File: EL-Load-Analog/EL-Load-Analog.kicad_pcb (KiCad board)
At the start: 4 copper layers, 185 x 95 mm, 282 parts, among them J1 Fan PWM, J101 Conn_01x10_Male, J102 JST-XH 2-pin, J103 JST-XH 2-pin, J104 Conn_02x12_Counter_Clockwise, J301 VSense, Q101 TIP42C, Q201 2N7002, Q202 2N7002, Q203 IRFP250M, Q204 IRFP250M, Q205 2N7002, Q206 2N7002, Q207 IRFP250M, Q208 IRFP250M, Q301 2N7002, Q302 BSS138, Q401 BSS138, U1 ADS1115IDGS, U101 AMS1117-3.3, U102 ADM1032, U2 MAX31760, U201 LM318D, U202 LM318D, U203 MCP6V51/LTC2050HV, U204 MCP6V51/LTC2050HV, U205 LM318D, U206 LM318D, U207 MCP6V51/LTC2050HV, U208 MCP6V51/LTC2050HV, U3 BD00FC0WFP-E2, U301 LM833, U302 LM833, U303 OPA189/MCP6V51/LTC2050HV, U304 OPA189/MCP6V51/LTC2050HV, U305 74HCT02, U306 LM393, U401 AD8038, U402 LM393, U403 74HCT02, U501 TL431DBZ, U502 TL074, U503 TL074, U504 TL072

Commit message: Put REF2025 in place, added LICENSES and .gitignore
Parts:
- removed C105: 10u, Capacitor_SMD:C_0805_2012Metric_Pad1.18x1.45mm_HandSolder
- removed C106: 100n, Capacitor_SMD:C_0805_2012Metric_Pad1.18x1.45mm_HandSolder
- removed J102, J103: JST-XH 2-pin, Connector_JST:JST_XH_B2B-XH-A_1x02_P2.50mm_Vertical
- removed R501: 100, Resistor_SMD:R_0805_2012Metric_Pad1.20x1.40mm_HandSolder
- removed U501: TL431DBZ, Package_TO_SOT_SMD:SOT-23
- added C10: 1u, Capacitor_SMD:C_0805_2012Metric_Pad1.18x1.45mm_HandSolder, F.Cu at (76.2, 113.7)
- added C11: 22u, Capacitor_SMD:C_0805_2012Metric_Pad1.18x1.45mm_HandSolder, F.Cu at (88.0, 111.0)
- added C12: 1u, Capacitor_SMD:C_0805_2012Metric_Pad1.18x1.45mm_HandSolder, F.Cu at (93.0, 109.0)
- added U4: REF5025AD, Package_SO:SOIC-8_3.9x4.9mm_P1.27mm, F.Cu at (83.2, 112.0)
- moved C503 4.39 mm to (93.8, 112.8), turned to 90 degrees
- moved R502 1.42 mm to (95.2, 109.0)
- moved R504 1.34 mm to (97.1, 109.0)
- moved R506 1.33 mm to (101.2, 109.0)
- moved C504 1.31 mm to (99.1, 109.0)
- moved R508 1.25 mm to (103.1, 109.0)
- moved C508 1.00 mm to (90.2, 108.9)
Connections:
- C503 pad 1: Vref -> Net-(U4-Trim/NR)
- U502 pad 1: Vref -> unconnected-(U502-Pad1)
- U502 pad 2: Vref -> unconnected-(U502A---Pad2)
- U502 pad 3: Net-(U501-K) -> unconnected-(U502A-+-Pad3)
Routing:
- net +12P: track 329.3 -> 137.2 mm, vias 5 -> 4
- net Net-(U501-K): track 17.8 -> 0.00 mm, vias 2 -> 0
- net +5V: track 560.2 -> 576.3 mm, vias 19 -> 21
- net GND: track 399.6 -> 389.5 mm, vias 145 -> 149
- net Vref: track 43.5 -> 53.3 mm
- net Net-(U4-Trim/NR): track 0.00 -> 8.10 mm
- net SCL: track 188.6 -> 193.2 mm, vias 2 -> 4
- net Net-(U502B-+): track 21.2 -> 19.8 mm
- net -GCOM: track 165.8 -> 164.5 mm
- net +3.3V: track 459.9 -> 459.3 mm

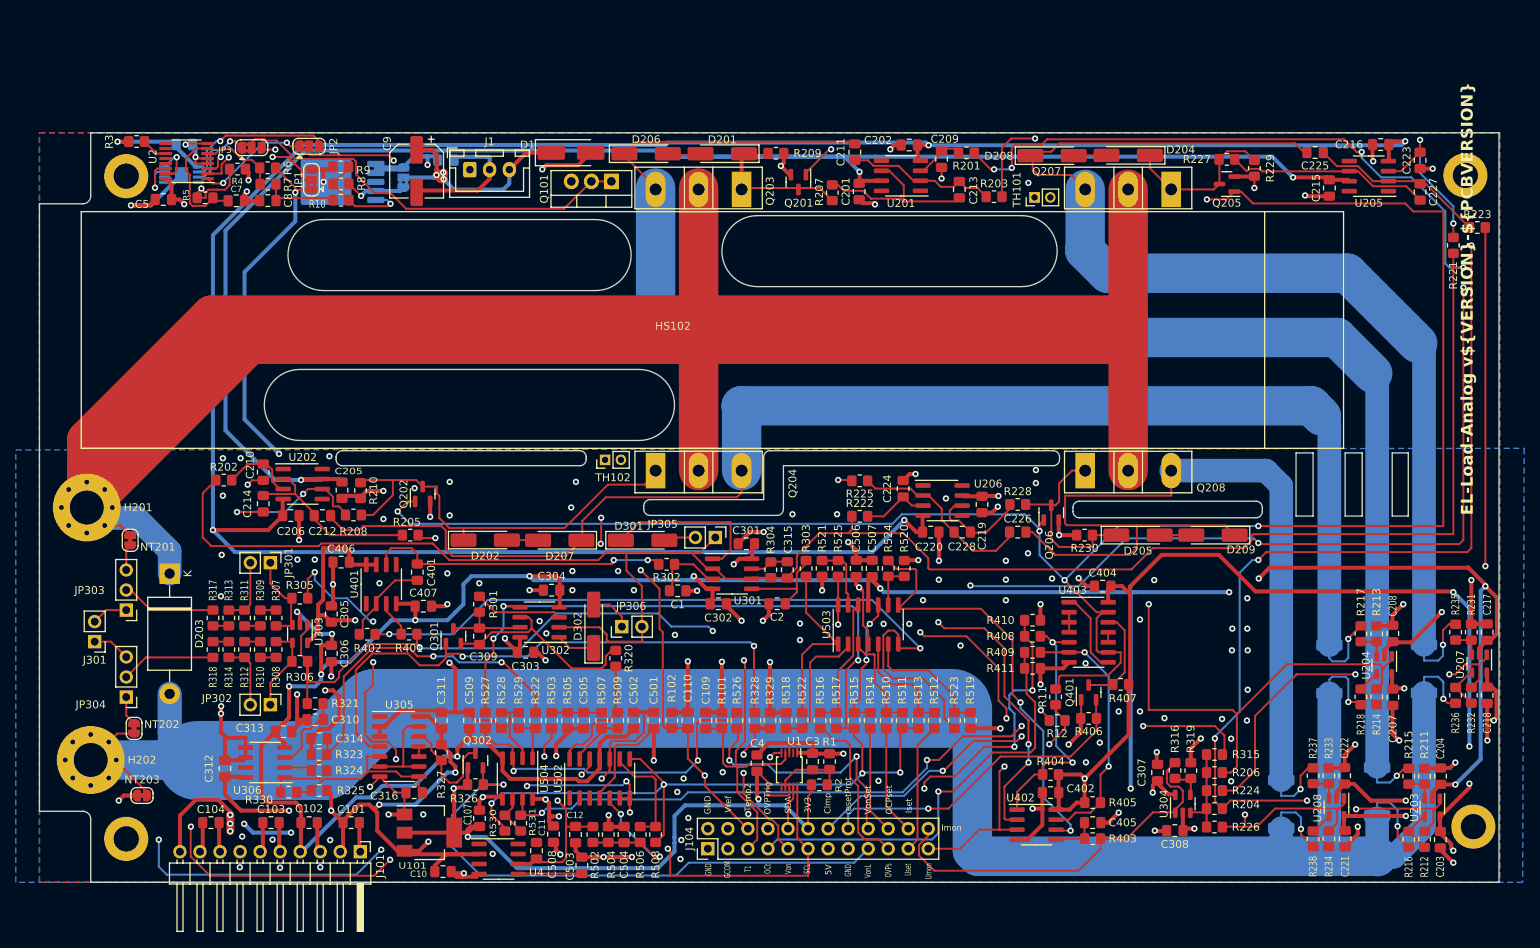
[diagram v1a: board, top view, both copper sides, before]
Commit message: Major Analog PCB update DAC/ADC + connectors included, fan IC removed
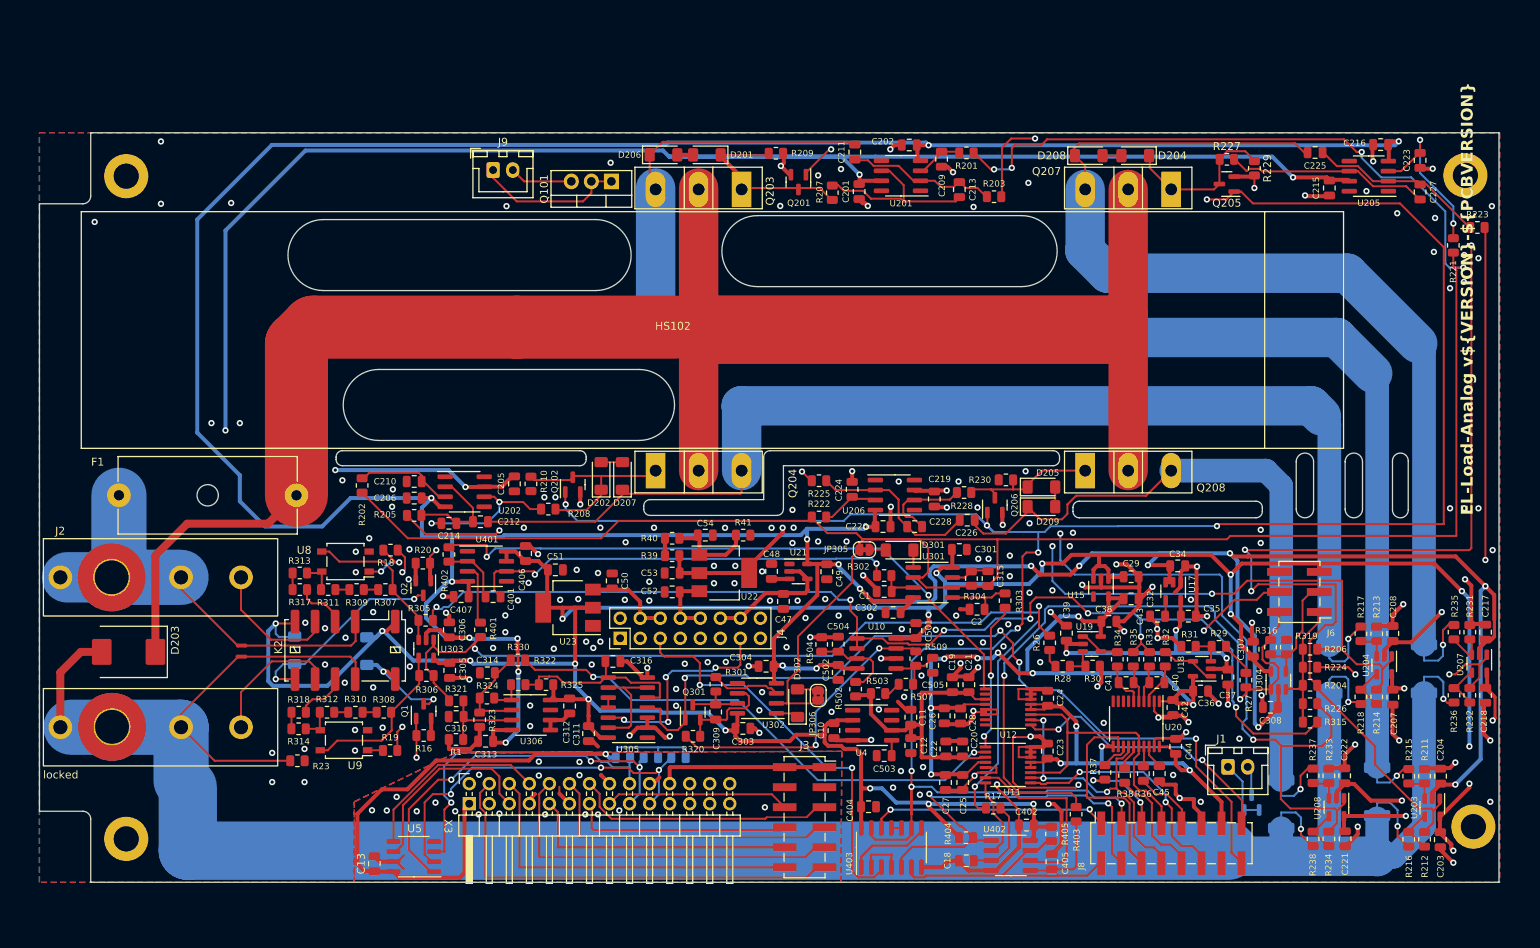
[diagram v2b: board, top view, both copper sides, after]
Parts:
- removed C101, C102, C103, C104, C107: 10u, Capacitor_SMD:C_0805_2012Metric_Pad1.18x1.45mm_HandSolder
- removed C108, C4, C5, C506, C507, C508, C509, C7: 100n, Capacitor_SMD:C_0805_2012Metric_Pad1.18x1.45mm_HandSolder
- removed C109, C110, C3, C6: 10n, Capacitor_SMD:C_0805_2012Metric_Pad1.18x1.45mm_HandSolder
- removed C8: 1u, Capacitor_SMD:C_0805_2012Metric_Pad1.18x1.45mm_HandSolder
- removed C9: 10u, Capacitor_SMD:CP_Elec_6.3x5.8
- removed D1: SS14, Diode_SMD:D_SMA_Handsoldering
- removed J101: Conn_01x10_Male, Connector_PinHeader_2.54mm:PinHeader_1x10_P2.54mm_Horizontal
- removed J104: Conn_02x12_Counter_Clockwise, Connector_PinHeader_2.54mm:PinHeader_2x12_P2.54mm_Vertical
- removed J301: VSense, Connector_PinHeader_2.54mm:PinHeader_1x02_P2.54mm_Vertical
- removed JP1: I2C Address, Jumper:SolderJumper-3_P1.3mm_Bridged2Bar12_RoundedPad1.0x1.5mm
- removed JP2, JP3, JP4: SolderJumper_3_Bridged12, Jumper:SolderJumper-3_P1.3mm_Bridged2Bar12_RoundedPad1.0x1.5mm
- removed JP301, JP302: Jumper_2_Open, Connector_PinHeader_2.54mm:PinHeader_1x02_P2.54mm_Vertical
- removed JP303, JP304: Jumper_3_Open, Connector_PinHeader_2.54mm:PinHeader_1x03_P2.54mm_Vertical
- removed NT203: NetTie_2, Jumper:SolderJumper-2_P1.3mm_Bridged_RoundedPad1.0x1.5mm
- removed Q302, Q401: BSS138, Package_TO_SOT_SMD:SOT-23
- removed R10, R101, R102, R9: 3k3, Resistor_SMD:R_0805_2012Metric_Pad1.20x1.40mm_HandSolder
- removed R11, R326, R327, R328, R406, R407, R408, R409, R506, R508, R510, R511, R512, R513, R514, R515, R516, R517, R518, R519, R520, R521, R522, R523, R524, R525, R526, R527, R528, R529: 10k, Resistor_SMD:R_0805_2012Metric_Pad1.20x1.40mm_HandSolder
- removed R12, R329, R410, R411, R530, R531: 20k, Resistor_SMD:R_0805_2012Metric_Pad1.20x1.40mm_HandSolder
- removed R2: 6k8, Resistor_SMD:R_0805_2012Metric_Pad1.20x1.40mm_HandSolder
- removed R3, R6: 4k7, Resistor_SMD:R_0805_2012Metric_Pad1.20x1.40mm_HandSolder
- removed R4, R7: 1k, Resistor_SMD:R_0805_2012Metric_Pad1.20x1.40mm_HandSolder
- removed R5: 10, Resistor_SMD:R_0805_2012Metric_Pad1.20x1.40mm_HandSolder
- removed R505: 15k, Resistor_SMD:R_0805_2012Metric_Pad1.20x1.40mm_HandSolder
- removed R8: 39k, Resistor_SMD:R_0805_2012Metric_Pad1.20x1.40mm_HandSolder
- removed TH101, TH102: Thermistor_NTC 10k, Connector_PinHeader_2.00mm:PinHeader_1x02_P2.00mm_Vertical
- removed U1: ADS1115IDGS, Package_SO:TSSOP-10_3x3mm_P0.5mm
- removed U101: AMS1117-3.3, Package_TO_SOT_SMD:SOT-223-3_TabPin2
- removed U102: ADM1032, Package_SO:MSOP-8-1EP_3x3mm_P0.65mm_EP1.68x1.88mm
- removed U2: MAX31760, Package_SO:QSOP-16_3.9x4.9mm_P0.635mm
- removed U3: BD00FC0WFP-E2, Package_TO_SOT_SMD:TO-252-5_TabPin6
- removed U502, U503: TL074, Package_SO:SO-14_3.9x8.65mm_P1.27mm
- removed U504: TL072, Package_SO:SO-8_3.9x4.9mm_P1.27mm
- added C13: 100n, Capacitor_SMD:C_0805_2012Metric, F.Cu at (67.5, 112.7)
- added C18: 10n, Capacitor_SMD:C_0805_2012Metric, F.Cu at (142.5, 112.3)
- added C19: 1u, Capacitor_SMD:C_0805_2012Metric, F.Cu at (140.7, 90.0)
- added C20: 1u, Capacitor_SMD:C_0805_2012Metric, F.Cu at (142.0, 98.1)
- added C21: 100n, Capacitor_SMD:C_0805_2012Metric, F.Cu at (142.8, 90.0)
- added C22: 100n, Capacitor_SMD:C_0805_2012Metric, F.Cu at (139.9, 98.1)
- added C23: 100n, Capacitor_SMD:C_0805_2012Metric, F.Cu at (152.8, 98.4)
- added C24: 100n, Capacitor_SMD:C_0805_2012Metric, F.Cu at (152.8, 91.7)
- added C25: 100n, Capacitor_SMD:C_0805_2012Metric, F.Cu at (142.0, 102.3)
- added C26: 100n, Capacitor_SMD:C_0805_2012Metric, F.Cu at (139.7, 93.9)
- added C27: 10u, Capacitor_SMD:C_0805_2012Metric, F.Cu at (139.8, 102.3)
- added C28: 10u, Capacitor_SMD:C_0805_2012Metric, F.Cu at (141.8, 93.9)
- added C29: 1u, Capacitor_SMD:C_0805_2012Metric, F.Cu at (163.4, 76.3)
- added C32: 1u, Capacitor_SMD:C_0805_2012Metric, F.Cu at (163.4, 79.1)
- added C34: 2u2, Capacitor_SMD:C_0805_2012Metric, F.Cu at (169.3, 74.9)
- added C35: 2u2, Capacitor_SMD:C_0805_2012Metric, F.Cu at (170.6, 81.3)
- added C36: 100n, Capacitor_SMD:C_0805_2012Metric, F.Cu at (172.2, 90.8)
- added C37: 100n, Capacitor_SMD:C_0805_2012Metric, F.Cu at (175.7, 89.0)
- added C38: 100n, Capacitor_SMD:C_0805_2012Metric, F.Cu at (160.6, 81.9)
- added C39: 100n, Capacitor_SMD:C_0805_2012Metric, F.Cu at (155.2, 83.4)
- added C40: 10n, Capacitor_SMD:C_0805_2012Metric, F.Cu at (166.6, 89.7)
- added C41: 10n, Capacitor_SMD:C_0805_2012Metric, F.Cu at (162.7, 89.7)
- added C42: 1u, Capacitor_SMD:C_0805_2012Metric, F.Cu at (168.7, 92.8)
- added C43: 10n, Capacitor_SMD:C_0805_2012Metric, F.Cu at (166.7, 81.3)
- added C44: 1u, Capacitor_SMD:C_0805_2012Metric, F.Cu at (169.0, 97.8)
- added C45: 220n, Capacitor_SMD:C_0805_2012Metric, F.Cu at (166.9, 101.2)
- added C47: 1u, Capacitor_SMD:C_0805_2012Metric, F.Cu at (119.3, 79.4)
- added C48: 10n, Capacitor_SMD:C_0805_2012Metric, F.Cu at (117.8, 75.6)
- added C49: 10u, Capacitor_SMD:C_0805_2012Metric, F.Cu at (124.8, 75.6)
- added C50: 10u, Capacitor_SMD:C_0805_2012Metric, F.Cu at (97.6, 76.8)
- added C51: 22u, Capacitor_SMD:C_0805_2012Metric, F.Cu at (90.4, 75.4)
- added C52: 10u, Capacitor_SMD:C_0805_2012Metric, F.Cu at (105.2, 78.2)
- added C53: 22u, Capacitor_SMD:C_0805_2012Metric, F.Cu at (105.2, 75.8)
- added C54: 10n, Capacitor_SMD:C_0805_2012Metric, F.Cu at (109.4, 71.0)
- added D2: 1N4148, Diode_SMD:D_MiniMELF, B.Cu at (66.5, 85.7)
- added D3: 1N4148, Diode_SMD:D_MiniMELF, B.Cu at (57.4, 85.6)
- added F1: Fuse, Fuse:Fuseholder_Cylinder-5x20mm_Schurter_0031_8201_Horizontal_Open, F.Cu at (35.1, 66.0)
- added J2: Plus Terminal w. sense, Footprints:Deltron_Dual_4mm_572_0x00, F.Cu at (27.6, 76.3)
- added J3: Conn_02x06_Odd_Even, Connector_PinSocket_2.54mm:PinSocket_2x06_P2.54mm_Vertical_SMD, F.Cu at (122.0, 106.8)
- added J4: Conn_02x08_Odd_Even, Connector_PinHeader_2.54mm:PinHeader_2x08_P2.54mm_Vertical, F.Cu at (98.6, 84.1)
- added J6: Conn_02x03_Counter_Clockwise, Connector_PinHeader_2.54mm:PinHeader_2x03_P2.54mm_Vertical_SMD, F.Cu at (184.7, 78.2)
- added J8: Conn_02x08_Odd_Even, Connector_PinSocket_2.54mm:PinSocket_2x08_P2.54mm_Vertical_SMD, F.Cu at (168.5, 110.0)
- added J9: Temp Sensor heatsink, Connector_JST:JST_XH_B2B-XH-A_1x02_P2.50mm_Vertical, F.Cu at (82.5, 24.7)
- added K2: EE2-5TNU, Relay_SMD:Relay_DPDT_Kemet_EE2_NU_DoubleCoil, F.Cu at (63.8, 85.6)
- added Q1: 2N7002, Package_TO_SOT_SMD:SOT-23, F.Cu at (73.7, 93.3)
- added Q2: 2N7002, Package_TO_SOT_SMD:SOT-23, F.Cu at (73.7, 77.7)
- added Q4: MMBT3904, Package_TO_SOT_SMD:SOT-23, B.Cu at (178.7, 104.9)
- added R13: 10k, Resistor_SMD:R_0805_2012Metric, B.Cu at (102.5, 99.2)
- added R14: 10k, Resistor_SMD:R_0805_2012Metric, B.Cu at (106.0, 99.2)
- added R15: 10k, Resistor_SMD:R_0805_2012Metric, B.Cu at (99.0, 99.2)
- added R16: 100k, Resistor_SMD:R_0805_2012Metric, F.Cu at (73.7, 96.4)
- added R17: 10k, Resistor_SMD:R_0805_2012Metric, F.Cu at (145.9, 105.6)
- added R18: 100k, Resistor_SMD:R_0805_2012Metric, F.Cu at (69.5, 72.9)
- added R19: 100k, Resistor_SMD:R_0805_2012Metric, F.Cu at (69.5, 98.3)
- added R20: 100k, Resistor_SMD:R_0805_2012Metric, F.Cu at (73.6, 74.5)
- added R23: 0, Resistor_SMD:R_0805_2012Metric, F.Cu at (57.7, 99.6)
- added R26: 100k 0.1%, Resistor_SMD:R_0805_2012Metric, F.Cu at (153.1, 84.7)
- added R27: 100k 0.1%, Resistor_SMD:R_0805_2012Metric, F.Cu at (177.9, 89.4)
- added R28: 10k 0.1%, Resistor_SMD:R_0805_2012Metric, F.Cu at (154.7, 87.6)
- added R29: 10k 0.1%, Resistor_SMD:R_0805_2012Metric, F.Cu at (174.5, 85.1)
- added R30: 100k 0.1%, Resistor_SMD:R_0805_2012Metric, F.Cu at (158.5, 87.6)
- added R31: 100k 0.1%, Resistor_SMD:R_0805_2012Metric, F.Cu at (170.7, 85.1)
- added R32: 1k, Resistor_SMD:R_0805_2012Metric, F.Cu at (167.7, 86.7)
- added R33: 1k, Resistor_SMD:R_0805_2012Metric, F.Cu at (165.7, 86.7)
- added R34: 1k, Resistor_SMD:R_0805_2012Metric, F.Cu at (161.6, 86.7)
- added R35: 1k, Resistor_SMD:R_0805_2012Metric, F.Cu at (163.7, 86.7)
- added R36: 47, Resistor_SMD:R_0805_2012Metric, F.Cu at (164.9, 101.2)
- added R37: 47, Resistor_SMD:R_0805_2012Metric, F.Cu at (160.1, 101.1)
- added R38: 47, Resistor_SMD:R_0805_2012Metric, F.Cu at (162.6, 101.5)
- added R39: 91, Resistor_SMD:R_0805_2012Metric, F.Cu at (105.2, 73.6)
- added R40: 1k8, Resistor_SMD:R_0805_2012Metric, F.Cu at (105.2, 71.4)
- added R41: 220, Resistor_SMD:R_0805_2012Metric, F.Cu at (114.2, 71.0)
- added U10: TL072/OPA2376, Package_SO:SOIC-8_3.9x4.9mm_P1.27mm, F.Cu at (131.1, 86.0)
- added U11: DAC8555, Package_SO:TSSOP-16_4.4x5mm_P0.65mm, F.Cu at (147.8, 100.1)
- added U12: DAC8555, Package_SO:TSSOP-16_4.4x5mm_P0.65mm, F.Cu at (147.8, 92.8)
- added U15: TPS7A2030, Package_TO_SOT_SMD:SOT-23-5, F.Cu at (159.6, 77.7)
- added U17: TPS72325, Package_TO_SOT_SMD:SOT-23-5, F.Cu at (168.7, 78.1)
- added U18: MCP6V51, Package_TO_SOT_SMD:SOT-23-5, F.Cu at (172.3, 87.9)
- added U19: MCP6V51, Package_TO_SOT_SMD:SOT-23-5, F.Cu at (158.4, 84.8)
- added U20: ADS131M02, Package_SO:TSSOP-20_4.4x6.5mm_P0.65mm, F.Cu at (164.0, 94.9)
- added U21: LT1964-5, Package_TO_SOT_SMD:TSOT-23-5, F.Cu at (121.2, 75.6)
- added U22: AMS1117, Package_TO_SOT_SMD:SOT-223-3_TabPin2, F.Cu at (111.8, 75.8)
- added U23: TLV1117-50, Package_TO_SOT_SMD:SOT-223-3_TabPin2, F.Cu at (92.0, 80.2)
- added U5: 24LC32, Package_SO:SO-8_3.9x4.9mm_P1.27mm, F.Cu at (72.5, 111.8)
- added U8: VO1400AEFTR, Package_SO:SO-4_4.4x4.3mm_P2.54mm, F.Cu at (63.8, 74.3)
- added U9: VO1400AEFTR, Package_SO:SO-4_4.4x4.3mm_P2.54mm, F.Cu at (63.6, 97.0)
- added X3: DIB Pheriperal connector, EEZ-DIB:DIB Pheriperal connector, F.Cu at (79.5, 105.1)
- added locked: Minus Terminal w. sense, Footprints:Deltron_Dual_4mm_572_0x00, F.Cu at (27.6, 95.3)
- C1, C10, C11, C12, C2, C201, C202, C203, C204, C205, C206, C207, C208, C209, C210, C211, C212, C213, C214, C215, C216, C217, C218, C219, C220, C221, C222, C223, C224, C225, C226, C227, C228, C301, C302, C303, C304, C305, C306, C307, C308, C309, C310, C311, C312, C313, C314, C315, C316, C401, C402, C404, C405, C406, C407, C501, C502, C503, C504, C505: footprint Capacitor_SMD:C_0805_2012Metric_Pad1.18x1.45mm_HandSolder -> Capacitor_SMD:C_0805_2012Metric
- D201, D202, D204, D205, D206, D207, D208, D209, D301, D302: footprint Diode_SMD:D_MiniMELF_Handsoldering -> Diode_SMD:D_MiniMELF
- D203: value 1.5KE100A -> 1.5KE100A smd variant; footprint Diode_THT:D_DO-201AE_P15.24mm_Horizontal -> Diode_SMD:D_SMC
- H201, H202: footprint MountingHole:MountingHole_4.3mm_M4_Pad_Via -> MountingHole:MountingHole_4.3mm_M4_Pad_TopBottom
- J1: value Fan PWM -> Temp Sensor PCB; footprint Connector_JST:JST_XH_B3B-XH-A_1x03_P2.50mm_Vertical -> Connector_JST:JST_XH_B2B-XH-A_1x02_P2.50mm_Vertical
- JP305: footprint Connector_PinHeader_2.54mm:PinHeader_1x02_P2.54mm_Vertical -> Jumper:SolderJumper-2_P1.3mm_Bridged_RoundedPad1.0x1.5mm
- JP306: footprint Connector_PinHeader_2.54mm:PinHeader_1x02_P2.54mm_Vertical -> Jumper:SolderJumper-2_P1.3mm_Bridged2Bar_RoundedPad1.0x1.5mm
- NT201, NT202: footprint Jumper:SolderJumper-2_P1.3mm_Bridged_RoundedPad1.0x1.5mm -> NetTie:NetTie-2_SMD_Pad0.5mm
- R1: value 3k3 -> 100k; footprint Resistor_SMD:R_0805_2012Metric_Pad1.20x1.40mm_HandSolder -> Resistor_SMD:R_0805_2012Metric
- R201, R202, R203, R204, R205, R206, R207, R208, R209, R210, R211, R212, R213, R214, R215, R216, R217, R218, R221, R222, R223, R224, R225, R226, R227, R228, R229, R230, R231, R232, R233, R234, R235, R236, R237, R238, R301, R302, R303, R304, R305, R306, R307, R308, R309, R310, R311, R312, R313, R314, R315, R316, R317, R318, R319, R320, R321, R322, R323, R324, R325, R330, R401, R402, R403, R404, R405, R502, R503, R504, R507, R509: footprint Resistor_SMD:R_0805_2012Metric_Pad1.20x1.40mm_HandSolder -> Resistor_SMD:R_0805_2012Metric
- moved J1 122.3 mm to (175.7, 100.4)
- moved C10 52.7 mm to (125.7, 95.8), turned to -90 degrees
- moved C11 50.4 mm to (135.4, 94.1)
- moved U4 50.3 mm to (130.6, 95.1)
- moved R1 47.4 mm to (77.8, 96.9), turned to 0 degrees
- moved C505 44.8 mm to (138.2, 87.5)
- moved C312 44.4 mm to (92.2, 92.7), turned to 90 degrees
- moved C12 44.0 mm to (135.4, 97.7)
- moved R503 41.5 mm to (131.3, 91.1), turned to 0 degrees
- moved C404 40.8 mm to (130.1, 105.4), turned to 180 degrees
- moved C503 40.8 mm to (132.1, 99.0), turned to 180 degrees
- moved R507 38.8 mm to (134.8, 89.9), turned to 0 degrees
- moved R509 38.6 mm to (136.1, 86.7)
- moved R502 38.1 mm to (128.4, 90.5), turned to 90 degrees
- moved U403 37.0 mm to (133.0, 110.6), turned to 90 degrees
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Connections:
- net LoopImon renamed /MOSFET Loops/LoopImon
- net LoopIset renamed /MOSFET Loops/LoopIset
- C202 pad 1: -5VA -> -5V
- C206 pad 1: -5VA -> -5V
- C216 pad 1: -5VA -> -5V
- C220 pad 1: -5VA -> -5V
- C505 pad 1: Net-(C505-Pad1) -> Net-(U10B-+)
- H201 pad 1: LoadPlus -> /MOSFET Loops/Plus
- J1 pad 1: /Tacho -> Net-(J1-Pin_1)
- J1 pad 2: GND -> Net-(J1-Pin_2)
- NT201 pad 2: LoadPlus -> /MOSFET Loops/Plus
- Q301 pad 1: Net-(Q301-G) -> ~{Von}
- R1 pad 2: Net-(U1-AIN3) -> Net-(U306A-+)
- R303 pad 2: CCsetOut -> Iset
- R315 pad 2: 4GCOM -> GCOM
- R322 pad 1: VonsetComp -> Vonset
- R402 pad 1: CVsetIn -> Uset
- R404 pad 1: Net-(R404-Pad1) -> OVPtriggered
- R405 pad 1: Net-(R405-Pad1) -> OCPtriggered
- R503 pad 2: Net-(C505-Pad1) -> Net-(R503-Pad2)
- R507 pad 1: Net-(C505-Pad1) -> Net-(R503-Pad2)
- R507 pad 2: Net-(U502D--) -> Net-(U10B-+)
- R509 pad 1: Net-(U502D--) -> Net-(U10B-+)
- U201 pad 4: -5VA -> -5V
- U202 pad 4: -5VA -> -5V
- U205 pad 4: -5VA -> -5V
- U206 pad 4: -5VA -> -5V
- U302 pad 5: -GCOM -> GND
- U305 pad 12: Net-(Q302-D) -> ~{VonLatch}
- U305 pad 4: Net-(Q301-G) -> ~{Von}
- U402 pad 1: Net-(R404-Pad1) -> OVPtriggered
- U402 pad 2: OVPsetComp -> OVPset
- U402 pad 3: Umon -> Net-(U402A-+)
- U402 pad 6: OCPsetComp -> OCPset
- U402 pad 7: Net-(R405-Pad1) -> OCPtriggered
- U403 pad 12: Net-(Q401-D) -> resetProt
- U403 pad 3: Net-(U403-Pad2) -> HWProtEnable
- U403 pad 5: Net-(R404-Pad1) -> OVPtriggered
- U403 pad 6: Net-(R405-Pad1) -> OCPtriggered
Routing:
- net +3.3V: track 459.3 -> 0.00 mm, vias 11 -> 0
- net -5VA: track 353.8 -> 0.00 mm, vias 4 -> 0
- net Temp1: track 243.8 -> 0.00 mm, vias 4 -> 0
- net -5V: track 407.6 -> 610.6 mm, vias 17 -> 23
- net SCL: track 193.2 -> 0.00 mm, vias 4 -> 0
- net SDA: track 187.9 -> 0.00 mm, vias 3 -> 0
- net -GCOM: track 164.5 -> 0.00 mm, vias 7 -> 0
- net +12P: track 137.2 -> 0.00 mm, vias 4 -> 0
- net +5V: track 576.3 -> 444.3 mm, vias 21 -> 22
- net +3.0VA: track 0.00 -> 102.0 mm, vias 0 -> 8
- net 4GCOM: track 99.6 -> 0.00 mm, vias 4 -> 0
- net CVsetIn: track 97.5 -> 0.00 mm, vias 2 -> 0
- net GND: track 389.5 -> 300.2 mm, vias 149 -> 199
- net ~{Von}: track 22.3 -> 106.7 mm, vias 2 -> 4
- net +3.3V-DIB: track 0.00 -> 78.5 mm, vias 0 -> 1
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- added copper zone on F.Cu, net GND-DIB
- added copper zone on In1.Cu, net GND-DIB
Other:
- outline, holes or cut-outs redrawn
- board text removed: "3V3"
- board text removed: "5V"
- board text removed: "Clmp"
- board text removed: "GCOM"
- board text removed: "GND"
- board text removed: "Imon"
- board text removed: "Iset"
- board text removed: "OCPset"
- board text removed: "OCt"
- board text removed: "OVPTrig"
- board text removed: "OVPs"
- board text removed: "SCL"
- board text removed: "SDA"
- board text removed: "T1"
- board text removed: "Temp2"
- board text removed: "Umon"
- board text removed: "Uset"
- board text removed: "Von"
- board text removed: "VonL"
- board text removed: "VonSet"
- board text removed: "Vref"
- board text removed: "resetProt"
